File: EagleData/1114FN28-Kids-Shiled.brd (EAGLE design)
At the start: 86 x 53 mm, 19 parts

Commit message: Bord update
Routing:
- net N$4: track 0.67 -> 0.00 mm
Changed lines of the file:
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@@
 <setting verticaltext="up"/>
 </settings>
-<grid distance="50" unitdist="mil" unit="mil" style="lines" multiple="1" display="yes" altdistance="5" altunitdist="mil" altunit="mil"/>
+<grid distance="5" unitdist="mil" unit="mil" style="lines" multiple="1" display="yes" altdistance="5" altunitdist="mil" altunit="mil"/>
 <layers>
 <layer number="1" name="Top" color="4" fill="1" visible="yes" active="yes"/>
@@
 <text x="35.7124" y="4.8006" size="1.778" layer="51">PHOTO-IC</text>
 <text x="3.7465" y="13.7238" size="1.778" layer="25">dp21-(3.3v In)</text>
-<text x="3.6195" y="33.231" size="1.778" layer="25">TP1</text>
+<text x="3.3655" y="33.866" size="1.778" layer="25">TP1</text>
 <text x="8.5725" y="41.9178" size="1.778" layer="25">mbed 1114FN28</text>
 <hole x="2" y="50.97" drill="2.1"/>
@@
 <text x="3.7465" y="11.1838" size="1.778" layer="25">dp8-(AnalogGND)</text>
 <text x="1.0033" y="6.053" size="1.778" layer="25">dp7</text>
-<text x="79.651859375" y="7.50591875" size="1.778" layer="25" rot="R90">dp-18</text>
+<text x="79.651859375" y="6.61691875" size="1.778" layer="25" rot="R90">dp-18</text>
 <text x="82.191859375" y="7.50591875" size="1.778" layer="25" rot="R90">GND</text>
-<text x="84.731859375" y="7.50591875" size="1.778" layer="25" rot="R90">dp-24</text>
+<text x="84.731859375" y="6.61691875" size="1.778" layer="25" rot="R90">dp-24</text>
 <text x="67.1195" y="14.181" size="1.778" layer="25">TP2</text>
 </plain>
@@
 <elements>
 <element name="LED1" library="Aruduino-Kids-Shiled" package="LED5MM" value="I-06245-R" x="45.307" y="36.5203" smashed="yes">
-<attribute name="NAME" x="37.687" y="37.5617" size="1.27" layer="25" ratio="10"/>
+<attribute name="NAME" x="37.941" y="37.5617" size="1.27" layer="25" ratio="10"/>
 </element>
 <element name="LED2" library="Aruduino-Kids-Shiled" package="LED5MM" value="I-06245-G" x="45.3324" y="28.3923" smashed="yes">
-<attribute name="NAME" x="37.9664" y="30.0687" size="1.27" layer="25" ratio="10"/>
+<attribute name="NAME" x="37.973" y="31.75" size="1.27" layer="25" ratio="10"/>
 </element>
 <element name="0-50C" library="Aruduino-Kids-Shiled" package="NTC" value="NTC-103-AT-2" x="30.5435" y="10.4218" smashed="yes" rot="R180"/>
@@
 <contactref element="U$1" pad="P$28"/>
 <contactref element="LED2" pad="A"/>
-<wire x1="3.05308125" y1="41.783" x2="39.19024375" y2="41.783" width="0.4064" layer="16"/>
-<wire x1="39.19024375" y1="41.783" x2="40.005" y2="40.53644375" width="0.4064" layer="16" curve="-90"/>
+<wire x1="3.05308125" y1="41.783" x2="39.06324375" y2="41.783" width="0.4064" layer="16"/>
+<wire x1="39.06324375" y1="41.783" x2="40.005" y2="40.53644375" width="0.4064" layer="16" curve="-90"/>
 <wire x1="40.005" y1="40.53644375" x2="40.0304" y2="29.37706875" width="0.4064" layer="16"/>
 <wire x1="40.0304" y1="29.37706875" x2="41.11676875" y2="28.3923" width="0.4064" layer="16" curve="90"/>
 <wire x1="41.11676875" y1="28.3923" x2="44.0624" y2="28.3923" width="0.4064" layer="16"/>
-<wire x1="3.05308125" y1="41.783" x2="2.159" y2="42.29608125" width="0.4064" layer="16" curve="-90"/>
-<wire x1="2.159" y1="42.29608125" x2="2.159" y2="45.968921875" width="0.4064" layer="16"/>
+<wire x1="3.05308125" y1="41.783" x2="2.159" y2="42.55008125" width="0.4064" layer="16" curve="-90"/>
+<wire x1="2.159" y1="42.55008125" x2="2.159" y2="45.968921875" width="0.4064" layer="16"/>
 <wire x1="2.159" y1="47.9098" x2="2.159" y2="45.968921875" width="0.4064" layer="16"/>
 <wire x1="2.159" y1="45.968921875" x2="2.156459375" y2="45.96638125" width="0.4064" layer="16" curve="-90"/>
@@
 <wire x1="80.2386" y1="18.2118" x2="81.28" y2="17.1704" width="0.4064" layer="16" curve="-90"/>
 </signal>
-<signal name="N$4">
-<wire x1="44.57191875" y1="42.877740625" x2="45.239940625" y2="42.877740625" width="1.016" layer="16"/>
-</signal>
 <signal name="N$6">
 <wire x1="43.40098125" y1="42.872659375" x2="44.681140625" y2="42.872659375" width="1.016" layer="16"/>
@@
 <contactref element="U$8" pad="1"/>
 <contactref element="U$1" pad="P$1"/>
-<wire x1="2.159" y1="37.7498" x2="2.1844" y2="32.2072" width="0.4064" layer="16"/>
+<wire x1="2.1844" y1="32.2072" x2="2.159" y2="32.2072" width="0.4064" layer="16"/>
+<wire x1="2.159" y1="32.2072" x2="2.159" y2="37.7498" width="0.4064" layer="16"/>
 </signal>
 <signal name="N$25">

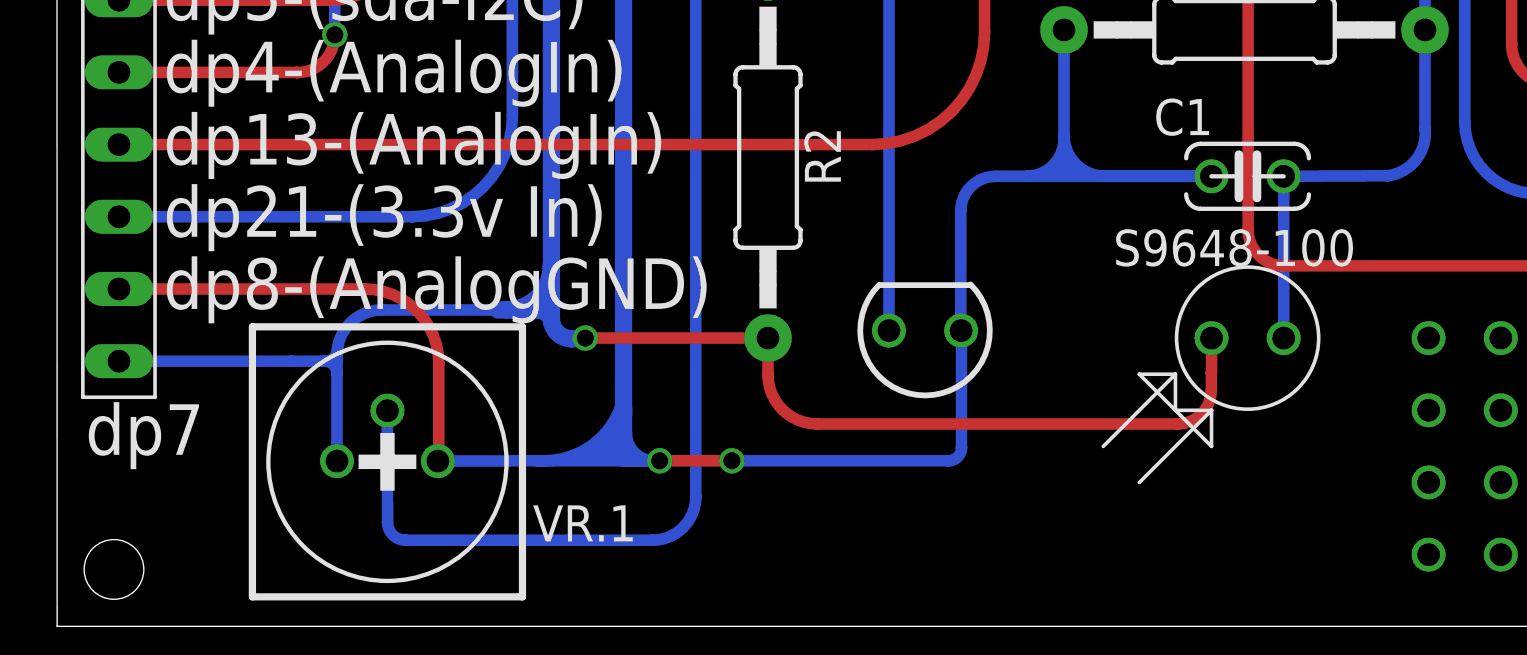
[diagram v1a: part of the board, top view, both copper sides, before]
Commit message: Change to FET part number.
I-6050 to I-6025 AKIZUKI part number.
IRLU3410PBF
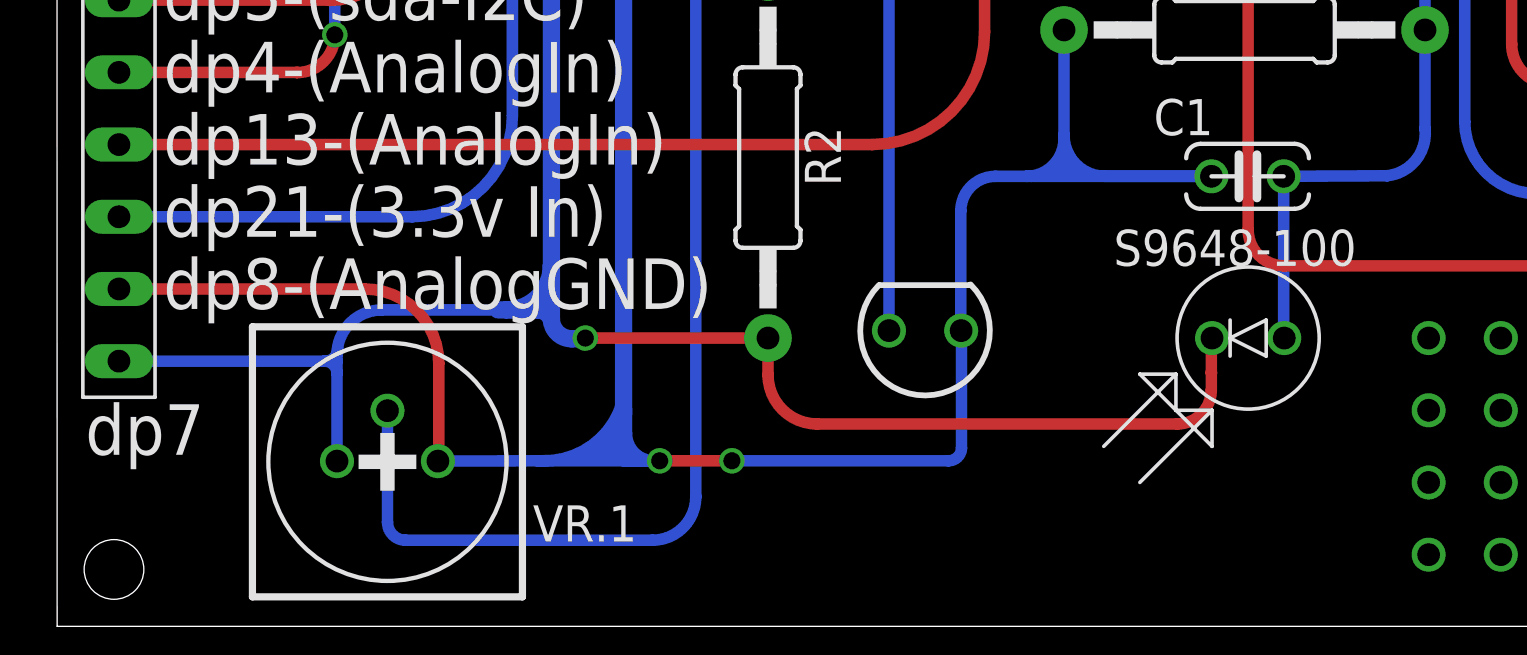
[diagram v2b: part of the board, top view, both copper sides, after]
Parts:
- U$2: device Aruduino-Kids-Shiled:PHOTO-IC -> 1114FN28-Kids-Shiled:PHOTO-IC
- U$4: value IR-6050 -> I-6025
- U$5: value IR6050 -> I-6025
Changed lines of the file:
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@@
 <setting verticaltext="up"/>
 </settings>
-<grid distance="5" unitdist="mil" unit="mil" style="lines" multiple="1" display="yes" altdistance="5" altunitdist="mil" altunit="mil"/>
+<grid distance="50" unitdist="mil" unit="mil" style="lines" multiple="1" display="yes" altdistance="5" altunitdist="mil" altunit="mil"/>
 <layers>
 <layer number="1" name="Top" color="4" fill="1" visible="yes" active="yes"/>
@@
 <attribute name="VALUE" x="16.8826625" y="1.1016" size="1.27" layer="27"/>
 </element>
-<element name="U$4" library="Aruduino-Kids-Shiled" package="TO251AA" value="IR-6050" x="60.2722" y="34.5" smashed="yes" rot="R90"/>
-<element name="U$5" library="Aruduino-Kids-Shiled" package="TO251AA" value="IR6050" x="60.2722" y="23.832" smashed="yes" rot="R90"/>
+<element name="U$4" library="Aruduino-Kids-Shiled" package="TO251AA" value="I-6025" x="60.2722" y="34.5" smashed="yes" rot="R90"/>
+<element name="U$5" library="Aruduino-Kids-Shiled" package="TO251AA" value="I-6025" x="60.2722" y="23.832" smashed="yes" rot="R90"/>
 <element name="U$1" library="Aruduino-Kids-Shiled" package="DIP28-SOCKET" value="FH-1X14" x="18.669" y="42.8298" smashed="yes" rot="R90"/>
-<element name="U$2" library="Aruduino-Kids-Shiled" package="PHOTO-IC" value="S9648-100" x="41.89221875" y="10.1576375" smashed="yes" rot="R180"/>
 <element name="C1" library="Aruduino-Kids-Shiled" package="C" value="0.1uF" x="41.89" y="15.85" smashed="yes">
 <attribute name="NAME" x="38.588" y="17.2978" size="1.27" layer="25" ratio="10"/>
@@
 <element name="U$8" library="1114FN28-Kids-Shiled" package="SIPS-10" value="SIPS-10" x="2.1844" y="20.7772"/>
 <element name="U$3" library="1114FN28-Kids-Shiled" package="SIPS-5" value="SIPS-5" x="78.74" y="15.24" rot="MR90"/>
+<element name="U$2" library="1114FN28-Kids-Shiled" package="PHOTO-IC" value="S9648-100" x="41.91" y="10.16" rot="R180"/>
 </elements>
 <signals>
@@
 <signal name="N$5">
 <contactref element="R1" pad="1"/>
-<contactref element="U$2" pad="P$1"/>
 <contactref element="C1" pad="2"/>
 <wire x1="48.133" y1="21" x2="48.133" y2="17.526" width="0.4064" layer="16"/>
@@
 <wire x1="48.133" y1="23.368" x2="48.133" y2="21" width="0.4064" layer="16"/>
 <wire x1="43.16" y1="15.85" x2="43.16221875" y2="15.84778125" width="0.4064" layer="16" curve="-90"/>
-<wire x1="43.16221875" y1="15.84778125" x2="43.16221875" y2="10.1576375" width="0.4064" layer="16"/>
+<contactref element="U$2" pad="P$1"/>
+<wire x1="43.18" y1="10.16" x2="43.16" y2="10.16" width="0.4064" layer="16"/>
+<wire x1="43.16" y1="10.16" x2="43.16" y2="15.85" width="0.4064" layer="16"/>
 </signal>
 <signal name="N$33">
@@
 <contactref element="VR.1" pad="P$3"/>
 <contactref element="U$1" pad="P$7"/>
-<contactref element="U$2" pad="P$2"/>
 <contactref element="R2" pad="1"/>
 <via x="18.5928" y="10.16" extent="1-16" drill="0.6"/>
@@
 <wire x1="15.8242" y1="11.1506" x2="17.399" y2="12.7254" width="0.6096" layer="16" curve="90"/>
 <wire x1="18.5928" y1="10.16" x2="25.019" y2="10.16" width="0.4064" layer="1"/>
-<wire x1="40.62221875" y1="10.1576375" x2="40.62221875" y2="8.94841875" width="0.4064" layer="1"/>
 <wire x1="40.62221875" y1="8.94841875" x2="40.6146" y2="8.9408" width="0.4064" layer="1" curve="-90"/>
 <wire x1="40.6146" y1="8.9408" x2="40.6146" y2="8.3312" width="0.4064" layer="1"/>
@@
 <wire x1="9.8556625" y1="9.3472" x2="9.8556625" y2="5.8306" width="0.4064" layer="16"/>
 <contactref element="U$8" pad="10"/>
-<wire x1="2.1844" y1="9.3472" x2="8.255" y2="9.3472" width="0.4064" layer="16"/>
-<wire x1="9.4234" y1="9.3472" x2="9.8556625" y2="9.3472" width="0.4064" layer="16"/>
+<wire x1="2.1844" y1="9.3472" x2="9.4234" y2="9.3472" width="0.4064" layer="16"/>
+<wire x1="9.4488" y1="9.3472" x2="9.8556625" y2="9.3472" width="0.4064" layer="16"/>
 <wire x1="9.8556625" y1="9.3472" x2="9.8556625" y2="9.5762625" width="0.4064" layer="16"/>
-<wire x1="8.255" y1="9.3472" x2="9.4234" y2="9.3472" width="0.4064" layer="16"/>
 <wire x1="9.4234" y1="9.3472" x2="9.8552" y2="8.9154" width="0.4064" layer="16" curve="-90"/>
 <wire x1="9.4234" y1="9.3472" x2="9.4488" y2="9.3472" width="0.4064" layer="16"/>
 <wire x1="9.4488" y1="9.3472" x2="9.8806" y2="9.779" width="0.4064" layer="16" curve="90"/>
+<contactref element="U$2" pad="P$2"/>
+<wire x1="40.64" y1="10.16" x2="40.6146" y2="10.16" width="0.4064" layer="1"/>
+<wire x1="40.6146" y1="10.16" x2="40.6146" y2="8.9408" width="0.4064" layer="1"/>
 </signal>
 <signal name="A-GND">

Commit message: Rev5
Rev5 update
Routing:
- net N$4: track 0.00 -> 20.1 mm
- net N$16: track 0.00 -> 18.4 mm
- net N$23: track 0.00 -> 15.6 mm
- net N$20: track 0.00 -> 13.0 mm
- net N$24: track 0.00 -> 1.51 mm
- added copper zone on layer 16, net GND
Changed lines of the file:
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@@
 <?xml version="1.0" encoding="utf-8"?>
 <!DOCTYPE eagle SYSTEM "eagle.dtd">
-<eagle version="6.6.0">
+<eagle version="7.2.0">
 <drawing>
 <settings>
@@
 <setting verticaltext="up"/>
 </settings>
-<grid distance="50" unitdist="mil" unit="mil" style="lines" multiple="1" display="yes" altdistance="5" altunitdist="mil" altunit="mil"/>
+<grid distance="5" unitdist="mil" unit="mil" style="lines" multiple="1" display="yes" altdistance="5" altunitdist="mil" altunit="mil"/>
 <layers>
 <layer number="1" name="Top" color="4" fill="1" visible="yes" active="yes"/>
@@
 <pass name="Default">
 <param name="RoutingGrid" value="50mil"/>
+<param name="AutoGrid" value="1"/>
+<param name="Efforts" value="0"/>
+<param name="TopRouterVariant" value="1"/>
 <param name="tpViaShape" value="round"/>
 <param name="PrefDir.1" value="0"/>
@@
 <via x="76.2" y="5.08" extent="1-16" drill="0.8"/>
 <via x="76.2" y="7.62" extent="1-16" drill="0.8"/>
+<wire x1="73.66" y1="7.62" x2="76.2" y2="7.62" width="0" layer="19" extent="1-1"/>
+<wire x1="76.2" y1="5.08" x2="76.2" y2="7.62" width="0" layer="19" extent="1-1"/>
+<wire x1="71.12" y1="7.62" x2="73.66" y2="7.62" width="0" layer="19" extent="1-1"/>
+<wire x1="73.66" y1="5.08" x2="73.66" y2="7.62" width="0" layer="19" extent="1-1"/>
+<wire x1="76.2" y1="2.54" x2="76.2" y2="5.08" width="0" layer="19" extent="1-1"/>
+<wire x1="73.66" y1="2.54" x2="73.66" y2="5.08" width="0" layer="19" extent="1-1"/>
 </signal>
 <signal name="N$19">
@@
 <wire x1="80.1116" y1="18.2118" x2="80.2386" y2="18.2118" width="0.4064" layer="16"/>
 <wire x1="80.2386" y1="18.2118" x2="81.28" y2="17.1704" width="0.4064" layer="16" curve="-90"/>
+<polygon width="0.4064" layer="16" isolate="0.4064">
+<vertex x="0" y="53.34"/>
+<vertex x="86.36" y="53.34"/>
+<vertex x="86.36" y="0"/>
+<vertex x="0" y="0"/>
+</polygon>
 </signal>
 <signal name="N$6">
@@
 <wire x1="19.939" y1="45.339" x2="19.939" y2="47.9098" width="0.4064" layer="1"/>
 </signal>
+<signal name="N$4">
+<wire x1="42.418" y1="43.561" x2="45.72" y2="43.561" width="0.254" layer="16"/>
+<wire x1="45.72" y1="43.561" x2="45.72" y2="43.434" width="0.254" layer="16"/>
+<wire x1="45.72" y1="43.434" x2="42.799" y2="43.434" width="0.254" layer="16"/>
+<wire x1="45.72" y1="43.434" x2="46.355" y2="43.434" width="0.254" layer="16"/>
+<wire x1="46.355" y1="43.434" x2="46.355" y2="43.307" width="0.254" layer="16"/>
+<wire x1="46.355" y1="43.307" x2="43.18" y2="43.307" width="0.254" layer="16"/>
+<wire x1="43.18" y1="43.307" x2="43.18" y2="43.688" width="0.254" layer="16"/>
+<wire x1="43.18" y1="43.688" x2="45.339" y2="43.688" width="0.254" layer="16"/>
+<wire x1="43.18" y1="43.688" x2="42.926" y2="43.688" width="0.254" layer="16"/>
+<wire x1="42.672" y1="43.688" x2="42.672" y2="43.434" width="0.254" layer="16"/>
+<wire x1="42.672" y1="43.434" x2="42.926" y2="43.434" width="0.254" layer="16"/>
+<wire x1="42.926" y1="43.434" x2="42.926" y2="43.688" width="0.254" layer="16"/>
+<wire x1="42.926" y1="43.688" x2="42.672" y2="43.688" width="0.254" layer="16"/>
+<wire x1="42.672" y1="43.434" x2="42.672" y2="42.418" width="0.254" layer="16"/>
+<wire x1="42.672" y1="42.418" x2="43.815" y2="42.418" width="0.254" layer="16"/>
+<wire x1="43.815" y1="42.418" x2="43.815" y2="41.783" width="0.254" layer="16"/>
+<wire x1="43.815" y1="41.783" x2="44.577" y2="41.783" width="0.254" layer="16"/>
+<wire x1="44.577" y1="41.783" x2="44.577" y2="42.164" width="0.254" layer="16"/>
+<wire x1="44.577" y1="42.164" x2="42.672" y2="42.164" width="0.254" layer="16"/>
+<wire x1="42.672" y1="42.164" x2="42.672" y2="42.291" width="0.254" layer="16"/>
+</signal>
+<signal name="N$16">
+<wire x1="43.942" y1="42.037" x2="43.053" y2="42.037" width="0.254" layer="16"/>
+<wire x1="44.323" y1="42.037" x2="43.942" y2="42.037" width="0.254" layer="16"/>
+<wire x1="43.942" y1="42.037" x2="43.942" y2="42.291" width="0.254" layer="16"/>
+<wire x1="43.942" y1="42.291" x2="44.704" y2="42.291" width="0.254" layer="16"/>
+<wire x1="44.831" y1="42.291" x2="44.704" y2="42.291" width="0.254" layer="16"/>
+<wire x1="44.704" y1="42.291" x2="44.704" y2="42.037" width="0.254" layer="16"/>
+<wire x1="44.704" y1="42.037" x2="44.831" y2="42.037" width="0.254" layer="16"/>
+<wire x1="45.466" y1="42.037" x2="44.831" y2="42.037" width="0.254" layer="16"/>
+<wire x1="44.831" y1="42.037" x2="44.831" y2="41.91" width="0.254" layer="16"/>
+<wire x1="45.974" y1="41.91" x2="44.831" y2="41.91" width="0.254" layer="16"/>
+<wire x1="44.831" y1="42.037" x2="44.831" y2="42.291" width="0.254" layer="16"/>
+<wire x1="44.831" y1="42.291" x2="45.72" y2="42.291" width="0.254" layer="16"/>
+<wire x1="45.72" y1="42.291" x2="45.72" y2="42.164" width="0.254" layer="16"/>
+<wire x1="45.72" y1="42.164" x2="44.958" y2="42.164" width="0.254" layer="16"/>
+<wire x1="44.958" y1="42.164" x2="44.958" y2="41.656" width="0.254" layer="16"/>
+<wire x1="44.958" y1="41.656" x2="45.212" y2="41.656" width="0.254" layer="16"/>
+<wire x1="47.625" y1="41.656" x2="45.212" y2="41.656" width="0.254" layer="16"/>
+<wire x1="45.212" y1="41.656" x2="45.212" y2="41.529" width="0.254" layer="16"/>
+<wire x1="45.212" y1="41.529" x2="47.879" y2="41.529" width="0.254" layer="16"/>
+<wire x1="47.879" y1="41.529" x2="47.879" y2="41.402" width="0.254" layer="16"/>
+<wire x1="47.879" y1="41.402" x2="47.752" y2="41.402" width="0.254" layer="16"/>
+<wire x1="47.752" y1="41.402" x2="47.752" y2="41.275" width="0.254" layer="16"/>
+<wire x1="47.752" y1="41.275" x2="45.212" y2="41.275" width="0.254" layer="16"/>
+<wire x1="45.212" y1="41.275" x2="45.212" y2="41.402" width="0.254" layer="16"/>
+<wire x1="45.212" y1="41.275" x2="45.212" y2="41.148" width="0.254" layer="16"/>
+<wire x1="45.212" y1="41.148" x2="47.625" y2="41.148" width="0.254" layer="16"/>
+<wire x1="47.625" y1="41.148" x2="47.625" y2="41.021" width="0.254" layer="16"/>
+</signal>
+<signal name="N$20">
+<wire x1="45.466" y1="40.894" x2="47.752" y2="40.894" width="0.254" layer="16"/>
+<wire x1="47.752" y1="40.894" x2="47.752" y2="40.767" width="0.254" layer="16"/>
+<wire x1="47.752" y1="40.767" x2="45.466" y2="40.767" width="0.254" layer="16"/>
+<wire x1="45.466" y1="40.767" x2="45.466" y2="40.513" width="0.254" layer="16"/>
+<wire x1="45.466" y1="40.513" x2="48.006" y2="40.513" width="0.254" layer="16"/>
+<wire x1="48.006" y1="40.513" x2="48.006" y2="40.259" width="0.254" layer="16"/>
+<wire x1="48.006" y1="40.259" x2="45.847" y2="40.259" width="0.254" layer="16"/>
+<wire x1="45.847" y1="40.259" x2="45.847" y2="40.386" width="0.254" layer="16"/>
+<wire x1="45.847" y1="40.386" x2="46.99" y2="40.386" width="0.254" layer="16"/>
+<wire x1="46.99" y1="40.386" x2="46.99" y2="42.164" width="0.254" layer="16"/>
+</signal>
+<signal name="N$23">
+<wire x1="78.994" y1="19.304" x2="80.264" y2="19.304" width="0.254" layer="16"/>
+<wire x1="80.264" y1="19.304" x2="80.264" y2="19.558" width="0.254" layer="16"/>
+<wire x1="80.264" y1="19.558" x2="78.867" y2="19.558" width="0.254" layer="16"/>
+<wire x1="78.867" y1="19.558" x2="78.867" y2="19.812" width="0.254" layer="16"/>
+<wire x1="80.137" y1="19.812" x2="78.867" y2="19.812" width="0.254" layer="16"/>
+<wire x1="78.867" y1="19.812" x2="78.867" y2="19.939" width="0.254" layer="16"/>
+<wire x1="78.867" y1="19.939" x2="80.137" y2="19.939" width="0.254" layer="16"/>
+<wire x1="78.867" y1="19.939" x2="78.74" y2="19.939" width="0.254" layer="16"/>
+<wire x1="78.74" y1="19.939" x2="78.74" y2="20.193" width="0.254" layer="16"/>
+<wire x1="78.74" y1="20.193" x2="80.264" y2="20.193" width="0.254" layer="16"/>
+<wire x1="80.264" y1="20.193" x2="80.264" y2="20.066" width="0.254" layer="16"/>
+<wire x1="80.264" y1="20.066" x2="78.994" y2="20.066" width="0.254" layer="16"/>
+<wire x1="78.994" y1="20.066" x2="78.994" y2="20.447" width="0.254" layer="16"/>
+<wire x1="78.994" y1="20.447" x2="79.883" y2="20.447" width="0.254" layer="16"/>
+<wire x1="79.883" y1="20.447" x2="79.883" y2="20.32" width="0.254" layer="16"/>
+<wire x1="79.883" y1="20.701" x2="79.883" y2="20.574" width="0.254" layer="16"/>
+<wire x1="79.883" y1="20.574" x2="80.264" y2="20.193" width="0.254" layer="16" curve="90"/>
+<wire x1="79.883" y1="20.574" x2="80.645" y2="19.812" width="0.254" layer="16" curve="90"/>
+<wire x1="80.264" y1="20.193" x2="80.645" y2="19.812" width="0.254" layer="16" curve="90"/>
+<wire x1="80.645" y1="19.812" x2="80.772" y2="19.812" width="0.254" layer="16"/>
+<wire x1="80.772" y1="19.812" x2="80.899" y2="19.685" width="0.254" layer="16" curve="-90"/>
+<wire x1="80.899" y1="19.685" x2="80.137" y2="19.685" width="0.254" layer="16"/>
+<wire x1="80.137" y1="19.685" x2="79.121" y2="20.701" width="0.254" layer="16" curve="-90"/>
+<wire x1="79.121" y1="20.701" x2="79.375" y2="20.701" width="0.254" layer="16"/>
+</signal>
+<signal name="N$24">
+<wire x1="79.756" y1="20.828" x2="79.756" y2="20.574" width="0.254" layer="16"/>
+<wire x1="79.756" y1="20.574" x2="80.645" y2="19.685" width="0.254" layer="16" curve="90"/>
+</signal>
 </signals>
